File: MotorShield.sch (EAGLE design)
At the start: 89 parts, among them IC1 OPA4340E, IC2 OPA4340E, IC3 74HCT125D

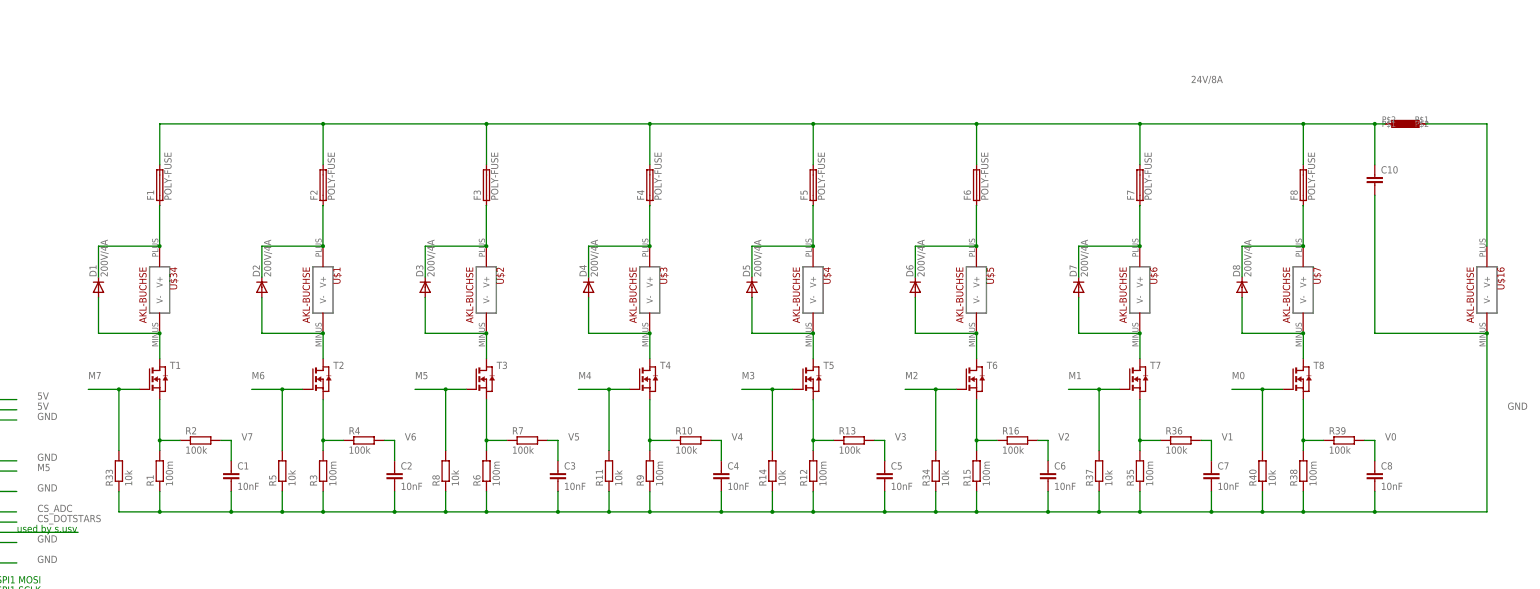
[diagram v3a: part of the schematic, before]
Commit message: changed connectors fixes #12
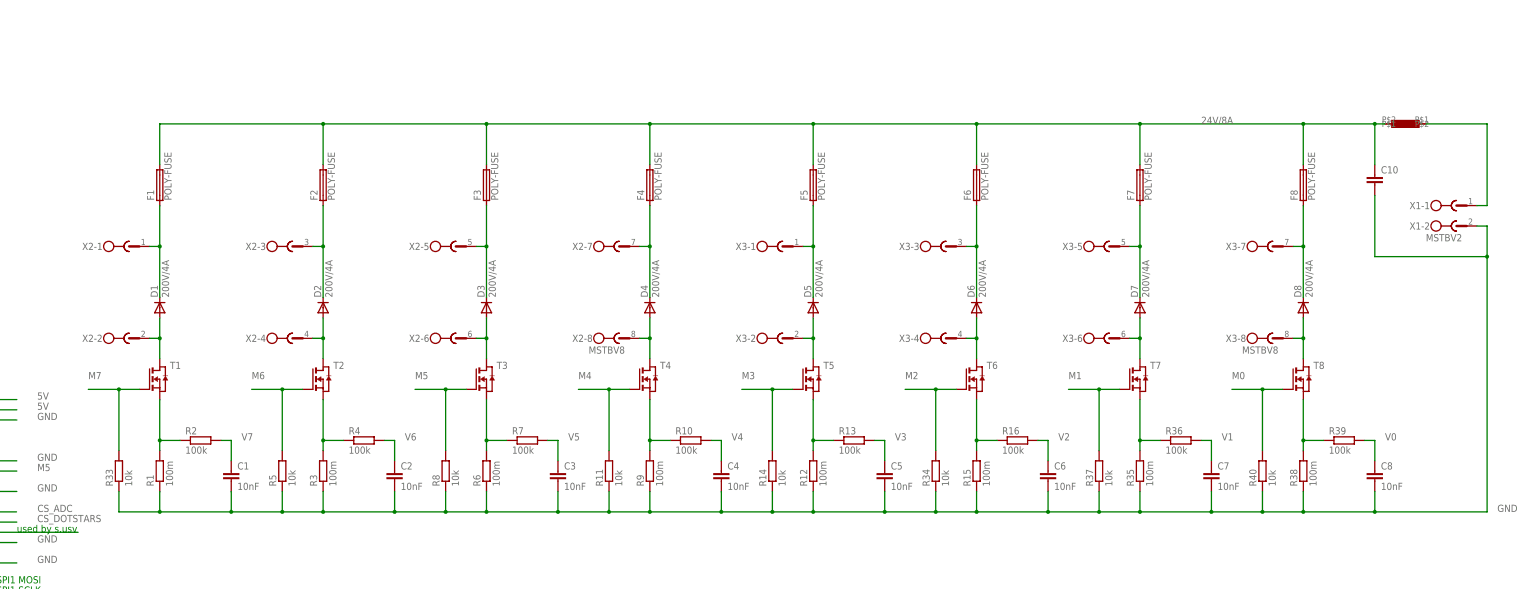
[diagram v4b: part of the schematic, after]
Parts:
- removed U$1, U$16, U$2, U$3, U$34, U$4, U$5, U$6, U$7: AKL-BUCHSE, Anschluss:AKL-BUCHSE
- added X1: MSTBV2, con-phoenix-508:MSTBV2
- added X2, X3: MSTBV8, con-phoenix-508:MSTBV8
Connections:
- removed net N$28: L1.P$1, U$16.V+
- new net N$23: L1.P$1, X1-1.1
- net 24V/1A: now also X2-1.1; no longer U$34.V+
- net GND: now also X1-2.1; no longer U$16.V-
- net N$10: now also X2-4.1; no longer U$1.V-
- net N$12: now also X2-5.1; no longer U$2.V+
- net N$13: now also X2-3.1; no longer U$1.V+
- net N$17: now also X2-6.1; no longer U$2.V-
- net N$2: now also X2-2.1; no longer U$34.V-
- net N$26: now also X2-8.1; no longer U$3.V-
- net N$38: now also X3-2.1; no longer U$4.V-
- net N$4: now also X3-7.1; no longer U$7.V+
- net N$45: now also X3-4.1; no longer U$5.V-
- net N$5: now also X3-5.1; no longer U$6.V+
- net N$51: now also X3-6.1; no longer U$6.V-
- net N$57: now also X3-8.1; no longer U$7.V-
- net N$7: now also X3-3.1; no longer U$5.V+
- net N$8: now also X3-1.1; no longer U$4.V+
- net N$9: now also X2-7.1; no longer U$3.V+
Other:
- moved on the sheet: D1, D2, D3, D4, D5, D6, D7, D8

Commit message: added connectors for inputs, button LED and dotstars fixes #7
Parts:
- added T9: (no value), transistor:BC847C-NPN-SOT23-BEC
- added X4: INPUTS, con-wago255:233-206
- added X5: BUTTON_LED, con-wago255:233-202
- added X6: DOTSTARS, con-wago255:233-203
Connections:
- removed net 24V/8A: C10.1, F1.2, F2.2, F3.2, F4.2, F5.2, F6.2, F7.2, F8.2, L1.P$2
- new net +24V: C10.1, F1.2, F2.2, F3.2, F4.2, F5.2, F6.2, F7.2, F8.2, L1.P$2, X5.-1
- new net INP_BTN_START: X4.-1
- new net INP_DOOR_CTRL: X4.-3
- new net INP_DOOR_JUICE: X4.-5
- new net N$32: T9.C, X5.-2
- new net N$33: T9.B
- net DOTCLK: now also X6.-2
- net DOTDAT: now also X6.-3
- net GND: now also T9.E, X4.-2, X4.-4, X4.-6, X6.-1

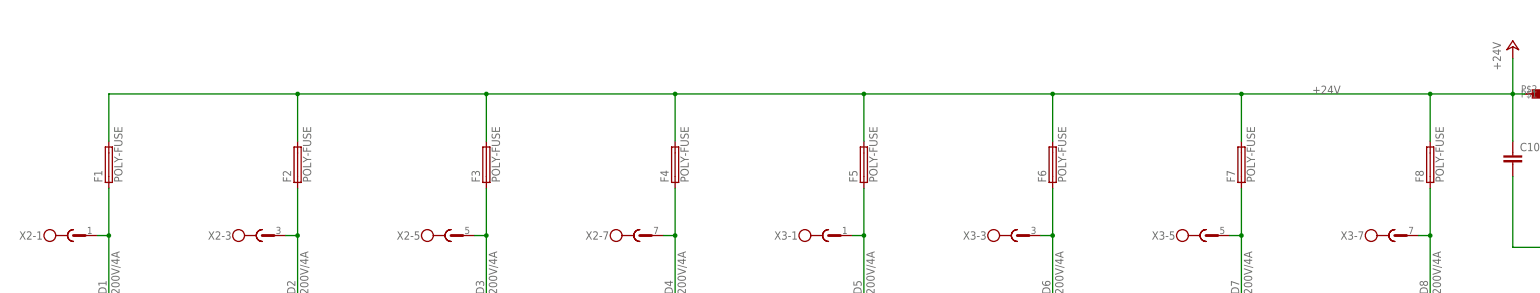
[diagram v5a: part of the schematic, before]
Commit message: changed fuse library to ptc-litlefuse from https://github.com/halfakop/eagle-lbr
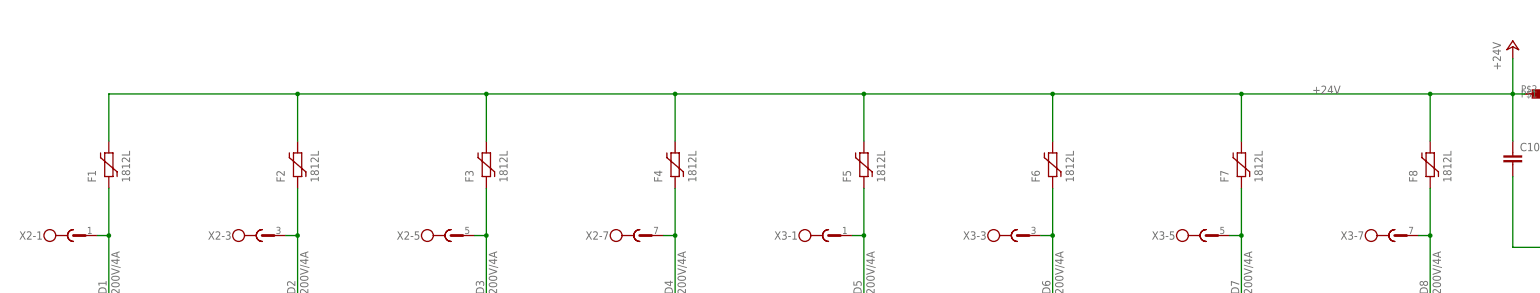
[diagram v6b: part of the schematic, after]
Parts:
- F1, F2, F3, F4, F5, F6, F7, F8: value POLY-FUSE -> 1812L; device SMD-Fuse:POLY-FUSE -> ptc-littlefuse:1812L

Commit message: added LEDs to indicate powered outputs and tripped fuses fixes #4, fixes #6
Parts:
- added LED1, LED11, LED13, LED15, LED3, LED5, LED7, LED9: red, led:LEDCHIP-LED0603
- added LED10, LED12, LED14, LED16, LED2, LED4, LED6, LED8: yellow, led:LEDCHIP-LED0603
- added R41, R42, R43, R44, R45, R46, R47, R48, R49, R50, R51, R52, R53, R54, R55, R56: (no value), rcl:R-EU_R0603
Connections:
- new net N$24: LED15.A, R55.1
- new net N$25: LED16.A, R56.1
- new net N$28: LED1.A, R41.1
- new net N$30: LED2.A, R42.1
- new net N$35: LED3.A, R43.1
- new net N$36: LED4.A, R44.1
- new net N$41: LED6.A, R46.1
- new net N$42: LED5.A, R45.1
- new net N$43: LED7.A, R47.1
- new net N$44: LED8.A, R48.1
- new net N$47: LED9.A, R49.1
- new net N$48: LED10.A, R50.1
- new net N$49: LED11.A, R51.1
- new net N$50: LED12.A, R52.1
- new net N$53: LED13.A, R53.1
- new net N$54: LED14.A, R54.1
- net +24V: now also R41.2, R42.2, R43.2, R44.2, R45.2, R46.2, R47.2, R48.2, R49.2, R50.2, R51.2, R52.2, R53.2, R54.2, R55.2, R56.2
- net 24V/1A: now also LED1.C
- net N$10: now also LED4.C
- net N$12: now also LED5.C
- net N$13: now also LED3.C
- net N$17: now also LED6.C
- net N$2: now also LED2.C
- net N$26: now also LED8.C
- net N$38: now also LED10.C
- net N$4: now also LED15.C
- net N$45: now also LED12.C
- net N$5: now also LED13.C
- net N$51: now also LED14.C
- net N$57: now also LED16.C
- net N$7: now also LED11.C
- net N$8: now also LED9.C
- net N$9: now also LED7.C
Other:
- moved on the sheet: C10, X1-1, X1-2

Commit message: exchanged MCP3008 symbol and footprint https://github.com/hpbock/PCB-Designs/blob/master/!Libraries/MCP3008.lbr
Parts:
- removed U$58: MCP3008SO16, MSC3008:MCP3008SO16
- added U$1: MCP3008SL, MCP3008:MCP3008SL
- C9: value 0,1uF -> 100nF; device eagle-ltspice:C -> rcl:C-EUC0805
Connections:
- removed net 3,3V: C9.1, IC1A.V+, IC2A.V+, PCB1.3V3@1, PCB1.3V3@2, U$58.VDD, U$58.VREF
- new net +3,3V: IC1A.V+, IC2A.V+, PCB1.3V3@1, PCB1.3V3@2
- new net +3V3: C9.1, U$1.VDD, U$1.VREF
- net CH0: now also U$1.CH0; no longer U$58.CH0
- net CH1: now also U$1.CH1; no longer U$58.CH1
- net CH2: now also U$1.CH2; no longer U$58.CH2
- net CH3: now also U$1.CH3; no longer U$58.CH3
- net CH4: now also U$1.CH4; no longer U$58.CH4
- net CH5: now also U$1.CH5; no longer U$58.CH5
- net CH6: now also U$1.CH6; no longer U$58.CH6
- net CH7: now also U$1.CH7; no longer U$58.CH7
- net CLK: now also U$1.SCK; no longer U$58.CLK
- net CS_ADC: now also U$1.!CS; no longer U$58.CS/SHDN
- net DIN: now also U$1.MOSI; no longer U$58.DIN
- net DOUT: now also U$1.MISO; no longer U$58.DOUT
- net GND: now also U$1.AGND, U$1.GND; no longer U$58.AGND, U$58.DGND
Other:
- moved on the sheet: C9
